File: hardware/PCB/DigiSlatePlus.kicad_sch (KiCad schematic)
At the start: 40 parts, among them J1 Serial, J10 IO7, J2 USB_B, J6 Mains, J7 Timecode IN, J8 Timecode OUT, J9 MISO, Q4 2N2222, SW1 RotaryEncoder-SW, SW2 1, SW3 1, SW4 1, SW5 1, SW6 BOOT, U1 ESP32-S3-WROOM-1, U2 DS3231M

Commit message: bugfixes in board
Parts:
- added D8: 1N4148, Diode_SMD:D_PowerDI-123, symbol Diode:1N4148
- added JP1: charge, Jumper:SolderJumper-2_P1.3mm_Open_TrianglePad1.0x1.5mm, symbol Jumper:Jumper_2_Open
- added R14: 220R, Resistor_SMD:R_1206_3216Metric, symbol Device:R
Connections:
- net +3.3V: now also R14.1
- net at BT1.1 (+), C3.1, U2.14 (VBAT): now also JP1.2 (B)
- new net: D8.1 (K), JP1.1 (A)
- new net: D8.2 (A), R14.2
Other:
- moved on the sheet: BT1, C2, C3, R5, R6, R7, U2

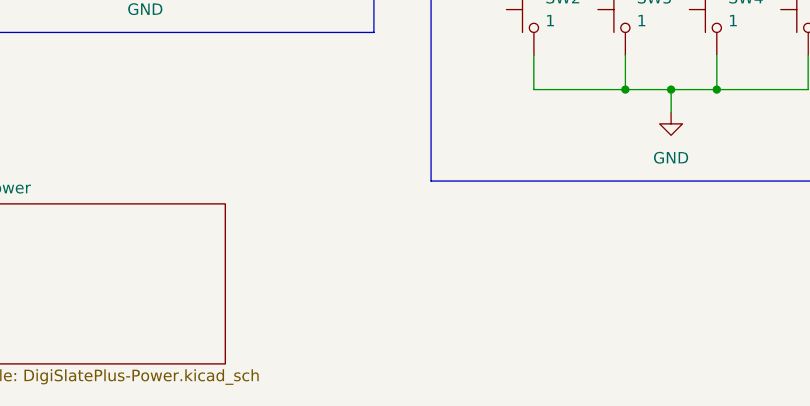
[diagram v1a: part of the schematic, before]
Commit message: dot matrix bugfixes
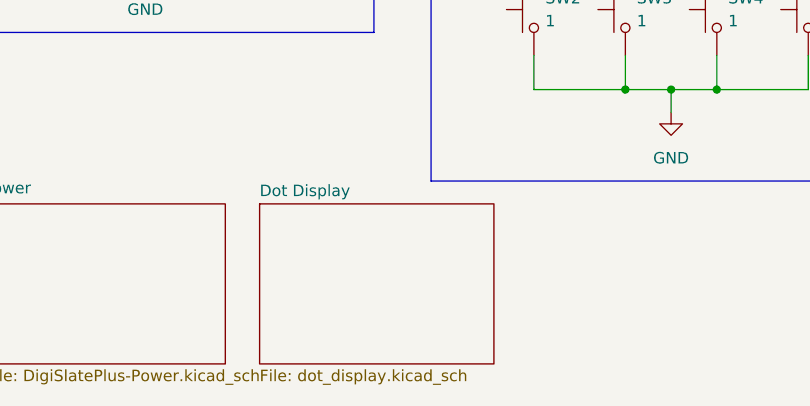
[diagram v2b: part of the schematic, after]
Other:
- added sheet Dot Display (dot_display.kicad_sch)
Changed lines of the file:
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@@
+		)
+	)
+	(sheet
+		(at 78.74 173.99)
+		(size 26.035 17.78)
+		(fields_autoplaced yes)
+		(stroke
+			(width 0.1524)
+			(type solid)
+		)
+		(fill
+			(color 0 0 0 0.0000)
+		)
+		(property "Sheetname" "Dot Display"
+			(at 78.74 173.2784 0)
+			(effects
+				(font
+					(size 1.27 1.27)
+				)
+				(justify left bottom)
+			)
+		)
+		(property "Sheetfile" "dot_display.kicad_sch"
+			(at 78.74 192.3546 0)
+			(effects
+				(font
+					(size 1.27 1.27)
+				)
+				(justify left top)
+			)
+		)
+		(instances
+			(project "DigiSlatePlus"
+				(path "/dcb9cf24-5afa-4bbe-8afa-a00529143e4d"
+					(page "4")
+				)
+			)
 		)
 	)

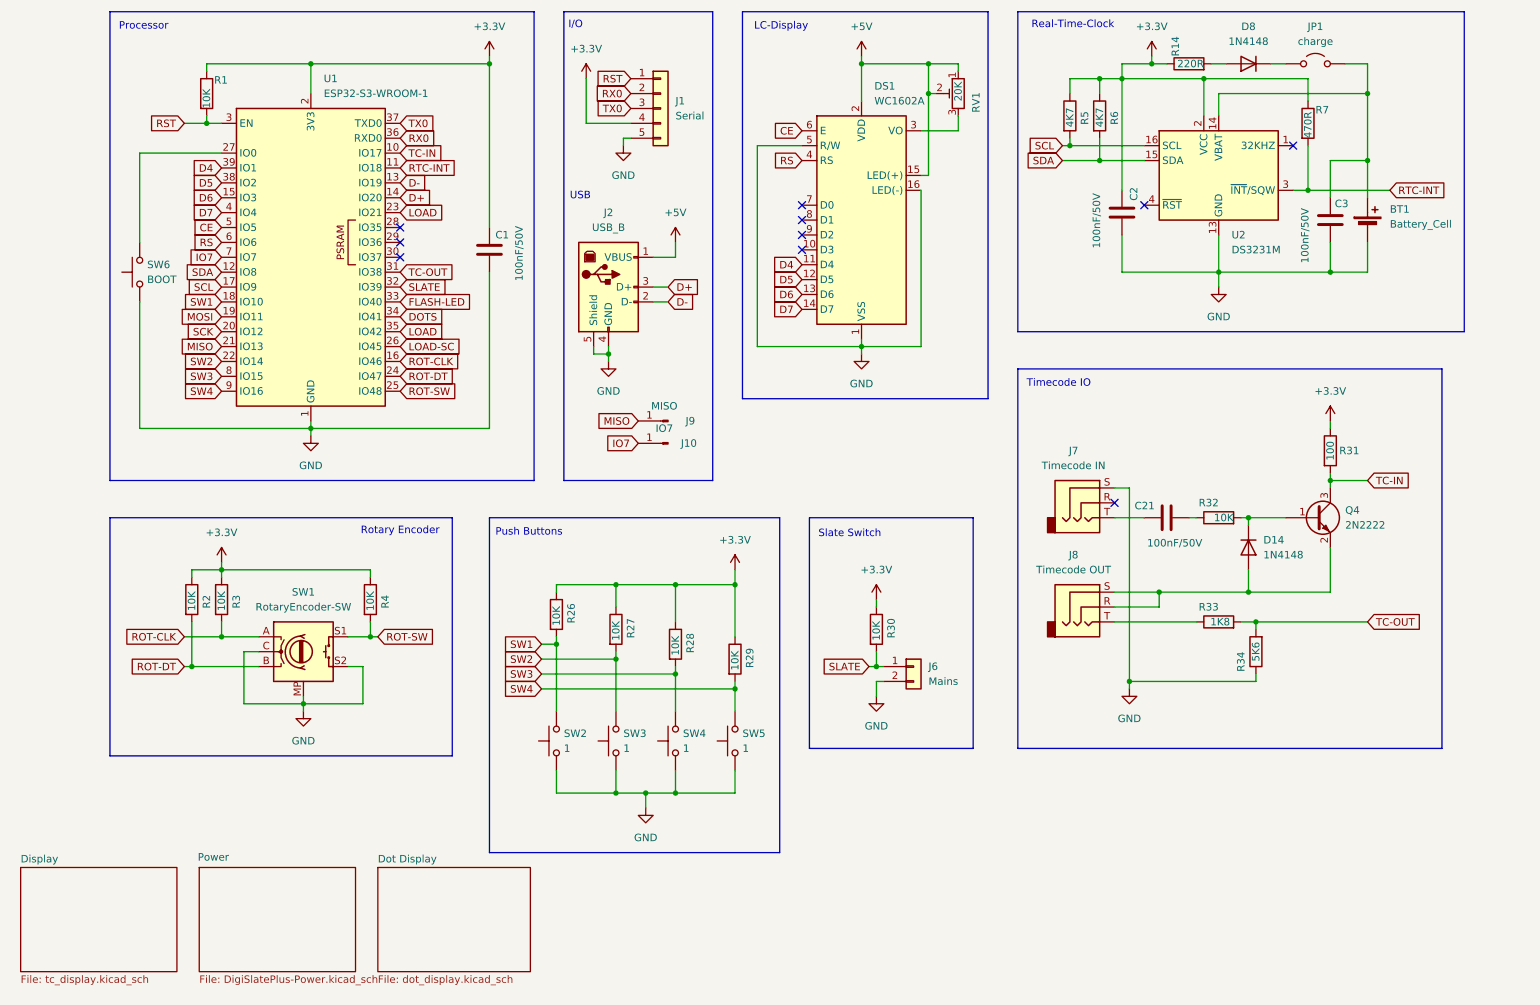
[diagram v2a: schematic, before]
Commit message: added KiCad libraries schematic bugfixes
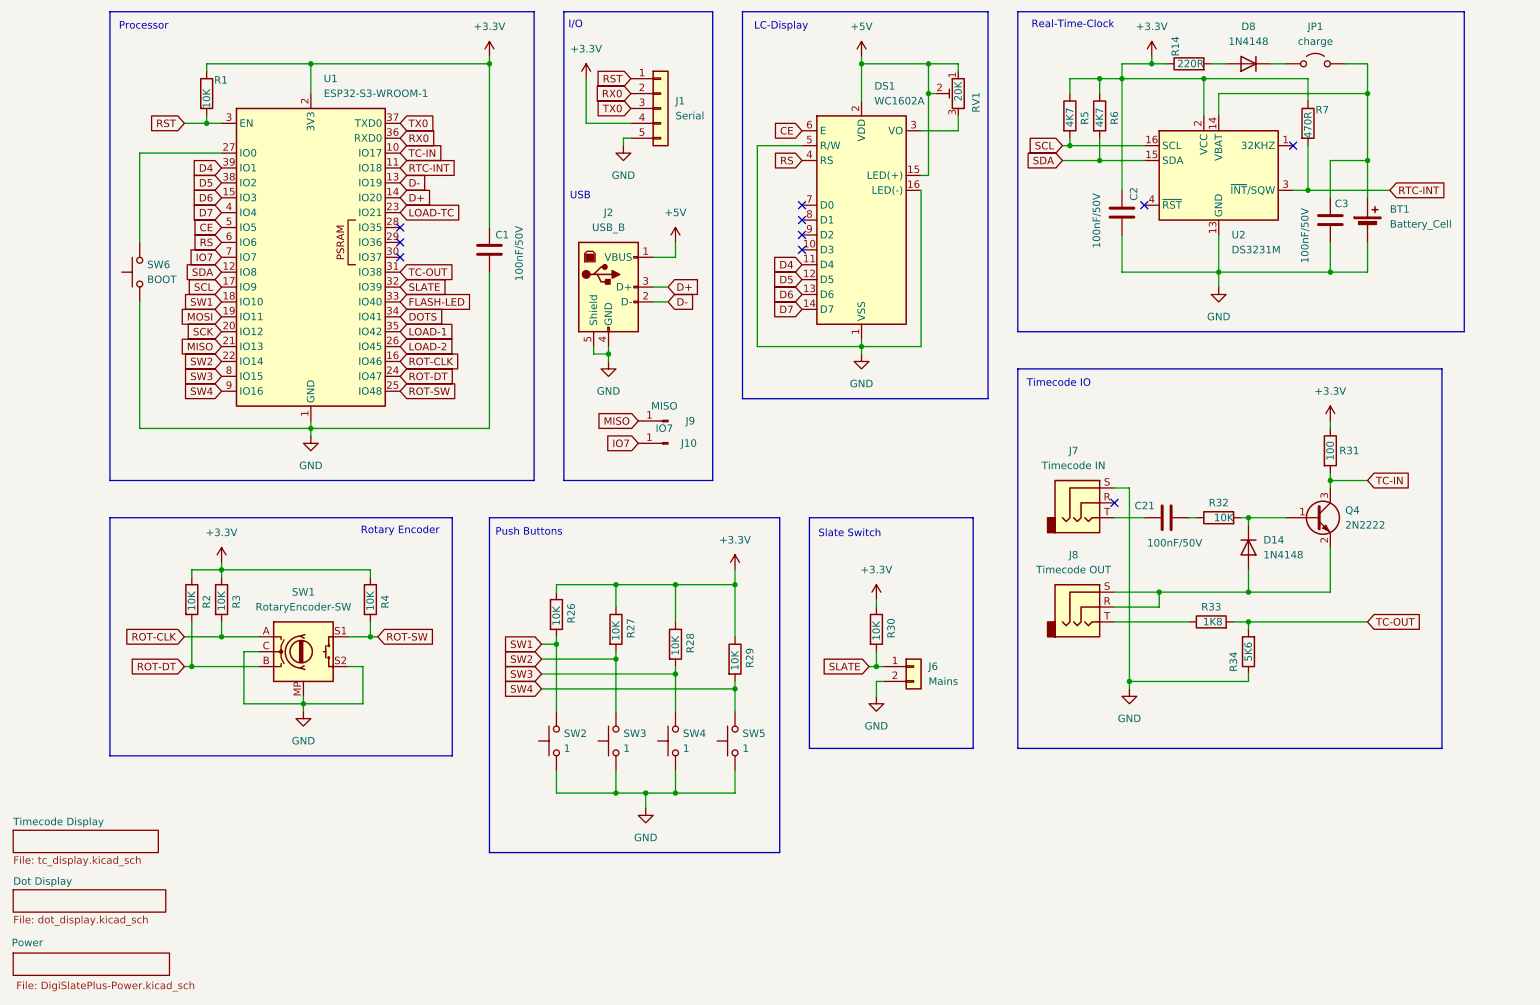
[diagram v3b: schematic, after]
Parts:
- BT1: footprint Battery:BatteryHolder_ComfortableElectronic_CH273-2450_1x2450 -> battery holder:BatteryHolder_ComfortableElectronic_CH273-2450_1x2450
- SW1: footprint Rotary_Encoder:RotaryEncoder_Bourns_Horizontal_PEC12R-2x17F-Sxxxx -> rotary:RotaryEncoder_Bourns_Horizontal
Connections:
- net LOAD renamed LOAD-1
- net LOAD-1: no longer U1.23 (IO21)
- net LOAD-SC renamed LOAD-2
- new net LOAD-TC: U1.23 (IO21)
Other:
- sheet Display renamed Timecode Display
- moved on the sheet: R33, R34
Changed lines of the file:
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@@
 	)
 	(junction
-		(at 228.6 132.08)
+		(at 227.33 132.08)
 		(diameter 0)
 		(color 0 0 0 0)
@@
 	(wire
 		(pts
-			(xy 226.06 132.08) (xy 228.6 132.08)
+			(xy 224.79 132.08) (xy 227.33 132.08)
 		)
 		(stroke
@@
 	(wire
 		(pts
-			(xy 228.6 132.08) (xy 228.6 133.35)
+			(xy 227.33 132.08) (xy 227.33 133.35)
 		)
 		(stroke
@@
 	(wire
 		(pts
-			(xy 228.6 140.97) (xy 228.6 142.24)
+			(xy 227.33 140.97) (xy 227.33 142.24)
 		)
 		(stroke
@@
 	(wire
 		(pts
-			(xy 228.6 132.08) (xy 247.65 132.08)
+			(xy 227.33 132.08) (xy 247.65 132.08)
 		)
 		(stroke
@@
 	(wire
 		(pts
-			(xy 228.6 142.24) (xy 207.01 142.24)
+			(xy 227.33 142.24) (xy 207.01 142.24)
 		)
 		(stroke
@@
 	(wire
 		(pts
-			(xy 204.47 132.08) (xy 218.44 132.08)
+			(xy 204.47 132.08) (xy 217.17 132.08)
 		)
 		(stroke
@@
 		)
 	)
-	(global_label "LOAD"
+	(global_label "LOAD-TC"
 		(shape input)
 		(at 82.55 62.23 0)
@@
 		)
 		(property "Intersheetrefs" "${INTERSHEET_REFS}"
-			(at 90.2524 62.23 0)
+			(at 94.0624 62.23 0)
 			(effects
 				(font
@@
 		)
 	)
-	(global_label "LOAD"
+	(global_label "LOAD-1"
 		(shape input)
 		(at 82.55 82.55 0)
@@
 		)
 		(property "Intersheetrefs" "${INTERSHEET_REFS}"
-			(at 90.2524 82.55 0)
+			(at 93.0343 82.55 0)
 			(effects
 				(font
@@
 		)
 	)
-	(global_label "LOAD-SC"
+	(global_label "LOAD-2"
 		(shape input)
 		(at 82.55 85.09 0)
@@
 		)
 		(property "Intersheetrefs" "${INTERSHEET_REFS}"
-			(at 94.3043 85.09 0)
+			(at 93.0343 85.09 0)
 			(effects
 				(font
@@
 	(symbol
 		(lib_id "Device:R")
-		(at 222.25 132.08 90)
+		(at 220.98 132.08 90)
 		(unit 1)
 		(exclude_from_sim no)
@@
 		(dnp no)
 		(property "Reference" "R33"
-			(at 222.25 129.54 90)
+			(at 220.98 129.54 90)
 			(effects
 				(font
 					(size 1.27 1.27)
 				)
-				(justify left)
 			)
 		)
 		(property "Value" "1K8"
-			(at 222.504 132.08 90)
+			(at 221.234 132.08 90)
 			(effects
 				(font
@@
 		)
 		(property "Footprint" "Resistor_SMD:R_1206_3216Metric"
-			(at 222.25 133.858 90)
+			(at 220.98 133.858 90)
 			(effects
 				(font
@@
 		)
 		(property "Datasheet" "~"
-			(at 222.25 132.08 0)
+			(at 220.98 132.08 0)
 			(effects
 				(font
@@
 		)
 		(property "Description" "Resistor"
-			(at 222.25 132.08 0)
+			(at 220.98 132.08 0)
 			(effects
 				(font
@@
 			)
 		)
-		(property "Footprint" "Battery:BatteryHolder_ComfortableElectronic_CH273-2450_1x2450"
+		(property "Footprint" "battery holder:BatteryHolder_ComfortableElectronic_CH273-2450_1x2450"
 			(at 247.65 63.246 90)
 			(effects
@@
 			)
 		)
-		(property "Footprint" "Rotary_Encoder:RotaryEncoder_Bourns_Horizontal_PEC12R-2x17F-Sxxxx"
+		(property "Footprint" "rotary:RotaryEncoder_Bourns_Horizontal"
 			(at 62.23 133.096 0)
 			(effects
@@
 					(size 1.27 1.27)
 				)
-				(justify left)
 			)
 		)
@@
 	(symbol
 		(lib_id "Device:R")
-		(at 228.6 137.16 180)
+		(at 227.33 137.16 180)
 		(unit 1)
 		(exclude_from_sim no)
@@
 		(dnp no)
 		(property "Reference" "R34"
-			(at 226.06 137.16 90)
+			(at 224.79 137.16 90)
 			(effects
 				(font
@@
 		)
 		(property "Value" "5K6"
-			(at 228.6 137.16 90)
+			(at 227.33 137.16 90)
 			(effects
 				(font
@@
 		)
 		(property "Footprint" "Resistor_SMD:R_1206_3216Metric"
-			(at 230.378 137.16 90)
+			(at 229.108 137.16 90)
 			(effects
 				(font
@@
 		)
 		(property "Datasheet" "~"
-			(at 228.6 137.16 0)
+			(at 227.33 137.16 0)
 			(effects
 				(font
@@
 		)
 		(property "Description" "Resistor"
-			(at 228.6 137.16 0)
+			(at 227.33 137.16 0)
 			(effects
 				(font
@@
 	)
 	(sheet
-		(at 17.78 173.99)
-		(size 26.67 17.78)
+		(at 16.51 167.64)
+		(size 24.765 3.81)
 		(fields_autoplaced yes)
 		(stroke
@@
 			(color 0 0 0 0.0000)
 		)
-		(property "Sheetname" "Display"
-			(at 17.78 173.2784 0)
+		(property "Sheetname" "Timecode Display"
+			(at 16.51 166.9284 0)
 			(effects
 				(font
@@
 		)
 		(property "Sheetfile" "tc_display.kicad_sch"
-			(at 17.78 192.3546 0)
+			(at 16.51 172.0346 0)
 			(effects
 				(font
@@
 	)
 	(sheet
-		(at 48.26 173.99)
-		(size 26.67 17.78)
+		(at 16.51 188.595)
+		(size 26.67 3.81)
 		(stroke
 			(width 0.1524)
@@
 		)
 		(property "Sheetname" "Power"
-			(at 48.006 172.974 0)
+			(at 16.256 187.579 0)
 			(effects
 				(font
@@
 		)
 		(property "Sheetfile" "DigiSlatePlus-Power.kicad_sch"
-			(at 48.26 192.3546 0)
+			(at 17.018 193.421 0)
 			(effects
 				(font
@@
 			(project "DigiSlatePlus"
 				(path "/dcb9cf24-5afa-4bbe-8afa-a00529143e4d"
-					(page "3")
+					(page "4")
 				)
 			)
@@
 	)
 	(sheet
-		(at 78.74 173.99)
-		(size 26.035 17.78)
+		(at 16.51 177.8)
+		(size 26.035 3.81)
 		(fields_autoplaced yes)
 		(stroke
@@
 		)
 		(property "Sheetname" "Dot Display"
-			(at 78.74 173.2784 0)
+			(at 16.51 177.0884 0)
 			(effects
 				(font
@@
 		)
 		(property "Sheetfile" "dot_display.kicad_sch"
-			(at 78.74 192.3546 0)
+			(at 16.51 182.1946 0)
 			(effects
 				(font
@@
 			(project "DigiSlatePlus"
 				(path "/dcb9cf24-5afa-4bbe-8afa-a00529143e4d"
-					(page "4")
+					(page "3")
 				)
 			)
